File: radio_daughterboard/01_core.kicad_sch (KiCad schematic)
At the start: 11 parts, among them J1 DF40C 60-pin radio daughterbo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, U1 AP2112K-3.3 600mA daughterboa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

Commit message: Apply BOM to radio + keyboard daughterboards, add Cherry MX switch 3D models
radio_daughterboard/:
- 74 MPNs assigned (33 resistors, 41 caps) across 4 schematic sheets
- 129 BOM gaps reduced to 7 (mounting holes H1-H4, DNP connectors J44/J72/J330)

12_keyboard_daughterboard/:
- 134 MPNs assigned: 65× 1N4148W-7-F diodes, 65× Cherry MX4A-L1NA switches,
  2× caps, 2× connectors
- BOM gaps eliminated: 134 → 0

3D models:
- Added Cherry_MX_ULP_SMD.step to ducktop2.3dshapes/ (65 Cherry MX switch
  footprints on keyboard daughterboard now have 3D models)
- Created gen/add_pcb_3d_models.py script for future 3D model assignments
- 57 footprints remain without models (MountingHole, TestPoint, Tag-Connect,
  and custom ducktop2 components — need manufacturer STEP files)

gen/:
- apply_bom_radio_daughterboard.py: radio daughterboard BOM catalog
- apply_bom_keyboard_daughterboard.py: keyboard daughterboard BOM catalog
- add_pcb_3d_models.py: automated 3D model path inserter
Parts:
- C1, C4: MPN (none) -> GRM31CR71E106KA12L; Manufacturer (none) -> Murata
- C2, C3: MPN (none) -> GRM21BR71A105KA01L; Manufacturer (none) -> Murata
- C5: MPN (none) -> GRM188R71H104KA93D; Manufacturer (none) -> Murata
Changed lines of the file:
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@@
   (property "Footprint" "Capacitor_SMD:C_1206_3216Metric" (at 400.05 88.9 0) (effects (font (size 1.27 1.27)) (hide yes)))
   (property "Datasheet" "" (at 400.05 88.9 0) (effects (font (size 1.27 1.27)) (hide yes)))
+  (property "Manufacturer" "Murata" (at 400.05 88.9 0) (effects (font (size 1.27 1.27)) (hide yes)))
+  (property "MPN" "GRM31CR71E106KA12L" (at 400.05 88.9 0) (effects (font (size 1.27 1.27)) (hide yes)))
   (pin "1")
   (pin "2")
@@
   (property "Footprint" "Capacitor_SMD:C_0805_2012Metric" (at 400.05 101.6 0) (effects (font (size 1.27 1.27)) (hide yes)))
   (property "Datasheet" "" (at 400.05 101.6 0) (effects (font (size 1.27 1.27)) (hide yes)))
+  (property "Manufacturer" "Murata" (at 400.05 101.6 0) (effects (font (size 1.27 1.27)) (hide yes)))
+  (property "MPN" "GRM21BR71A105KA01L" (at 400.05 101.6 0) (effects (font (size 1.27 1.27)) (hide yes)))
   (pin "1")
   (pin "2")
@@
   (property "Footprint" "Capacitor_SMD:C_0805_2012Metric" (at 400.05 114.3 0) (effects (font (size 1.27 1.27)) (hide yes)))
   (property "Datasheet" "" (at 400.05 114.3 0) (effects (font (size 1.27 1.27)) (hide yes)))
+  (property "Manufacturer" "Murata" (at 400.05 114.3 0) (effects (font (size 1.27 1.27)) (hide yes)))
+  (property "MPN" "GRM21BR71A105KA01L" (at 400.05 114.3 0) (effects (font (size 1.27 1.27)) (hide yes)))
   (pin "1")
   (pin "2")
@@
   (property "Footprint" "Capacitor_SMD:C_1206_3216Metric" (at 400.05 127 0) (effects (font (size 1.27 1.27)) (hide yes)))
   (property "Datasheet" "" (at 400.05 127 0) (effects (font (size 1.27 1.27)) (hide yes)))
+  (property "Manufacturer" "Murata" (at 400.05 127 0) (effects (font (size 1.27 1.27)) (hide yes)))
+  (property "MPN" "GRM31CR71E106KA12L" (at 400.05 127 0) (effects (font (size 1.27 1.27)) (hide yes)))
   (pin "1")
   (pin "2")
@@
   (property "Footprint" "Capacitor_SMD:C_0603_1608Metric" (at 400.05 139.7 0) (effects (font (size 1.27 1.27)) (hide yes)))
   (property "Datasheet" "" (at 400.05 139.7 0) (effects (font (size 1.27 1.27)) (hide yes)))
+  (property "Manufacturer" "Murata" (at 400.05 139.7 0) (effects (font (size 1.27 1.27)) (hide yes)))
+  (property "MPN" "GRM188R71H104KA93D" (at 400.05 139.7 0) (effects (font (size 1.27 1.27)) (hide yes)))
   (pin "1")
   (pin "2")

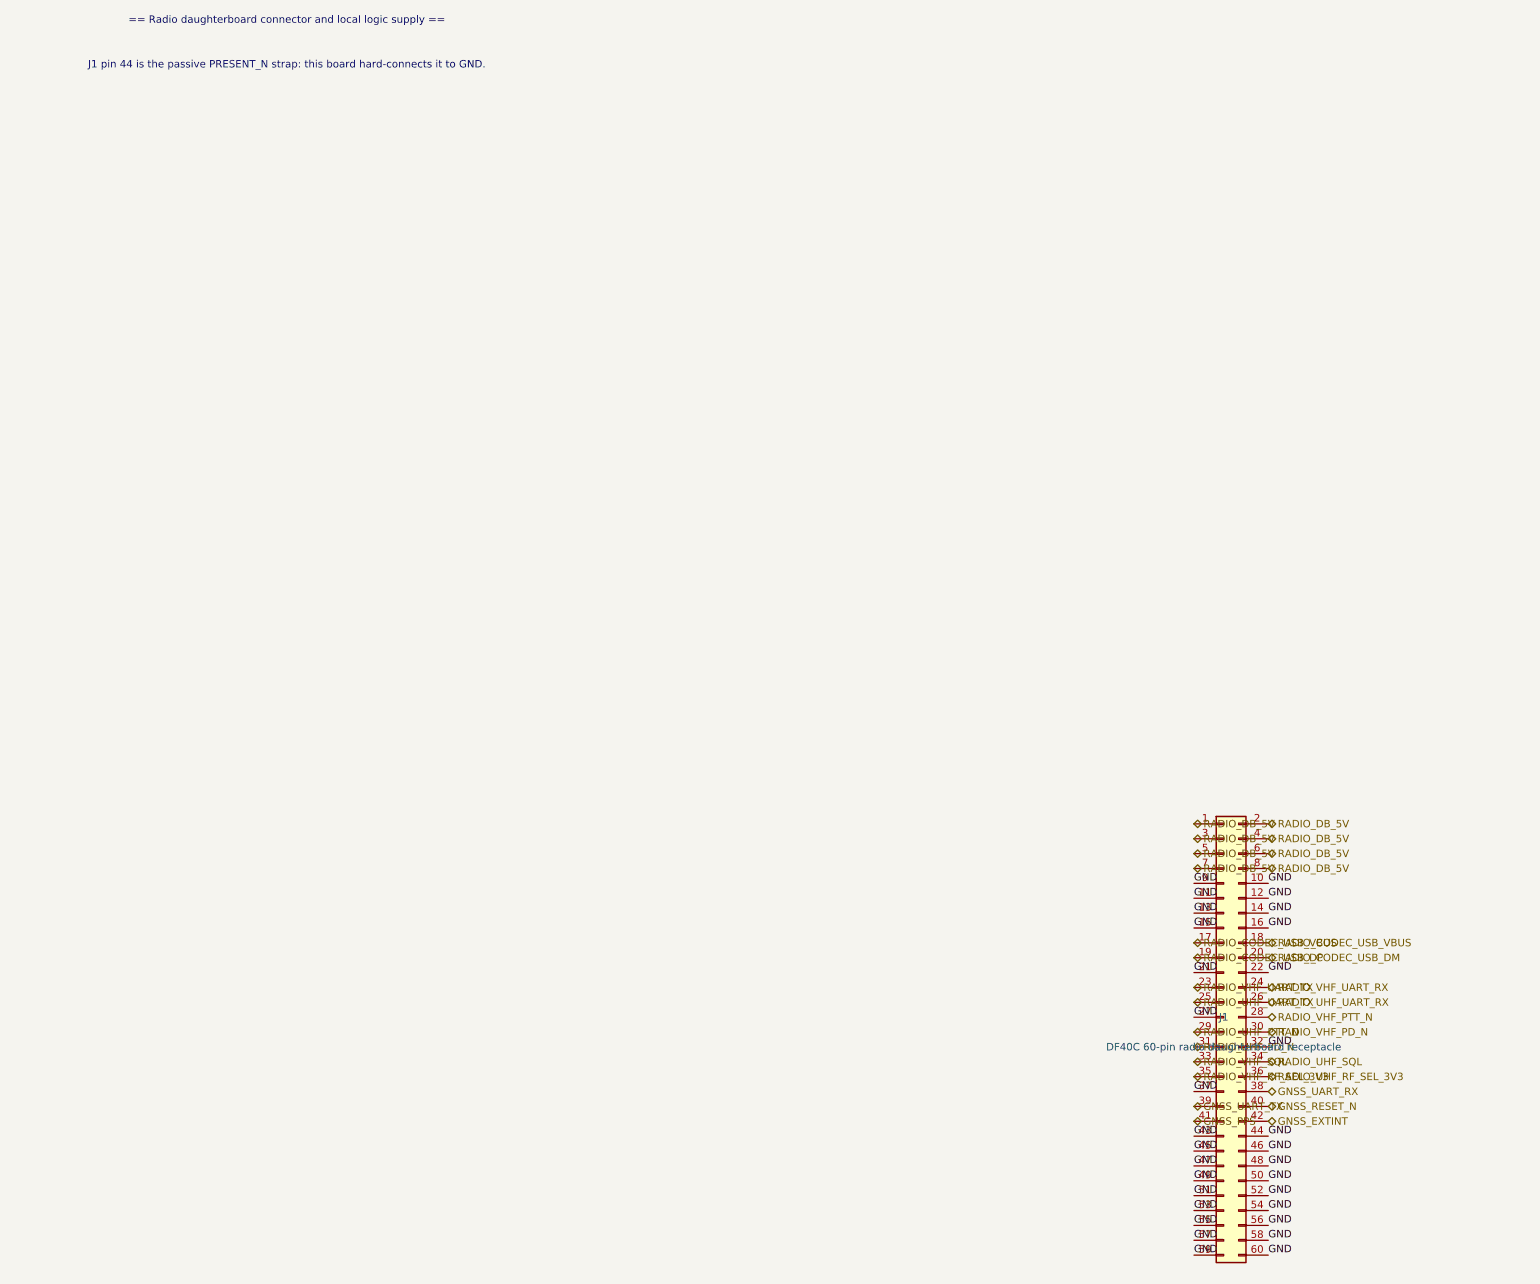
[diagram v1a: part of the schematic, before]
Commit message: Complete EC DFU port (J73) + DB power rework; verify schematic and board
- Add rear USB-C EC firmware programming port J73 (UFP/DFU) on Internal
  Services sheet: USBLC6-2P6 ESD (U63), 5.1k CC Rd resistors (R205/R211),
  22R series on D+/D- (R203/R204), mux-select hookup so BOOT0 high forces
  the USB mux to the DFU port
- Rename port ref J70->J73 after ham-radio collision; sync all net names
  (J73_CC1/J73_CC2)
- DB power rework: S5 gating + 3V3_STBY split, dual DCDC paths, GND
  returns on the standby rails; regenerate all sheets and re-verify
- sync_main_pcb_from_netlist: anchor placement for the 9 new footprints,
  scoped ECO support
- Board: rebuild main PCB with J73 footprint block (lib-sourced, net
  injection from netlist name attribute), sync pad nets for the 5 stale
  refs, remove duplicate R205/R211 copies
- Verified: check_schematic self-check OK (0 errors), radio DB contracts
  OK, ERC 0 errors, board DRC 0 electrical violations, board-vs-schematic
  net parity 0 conflicts, no duplicate refs
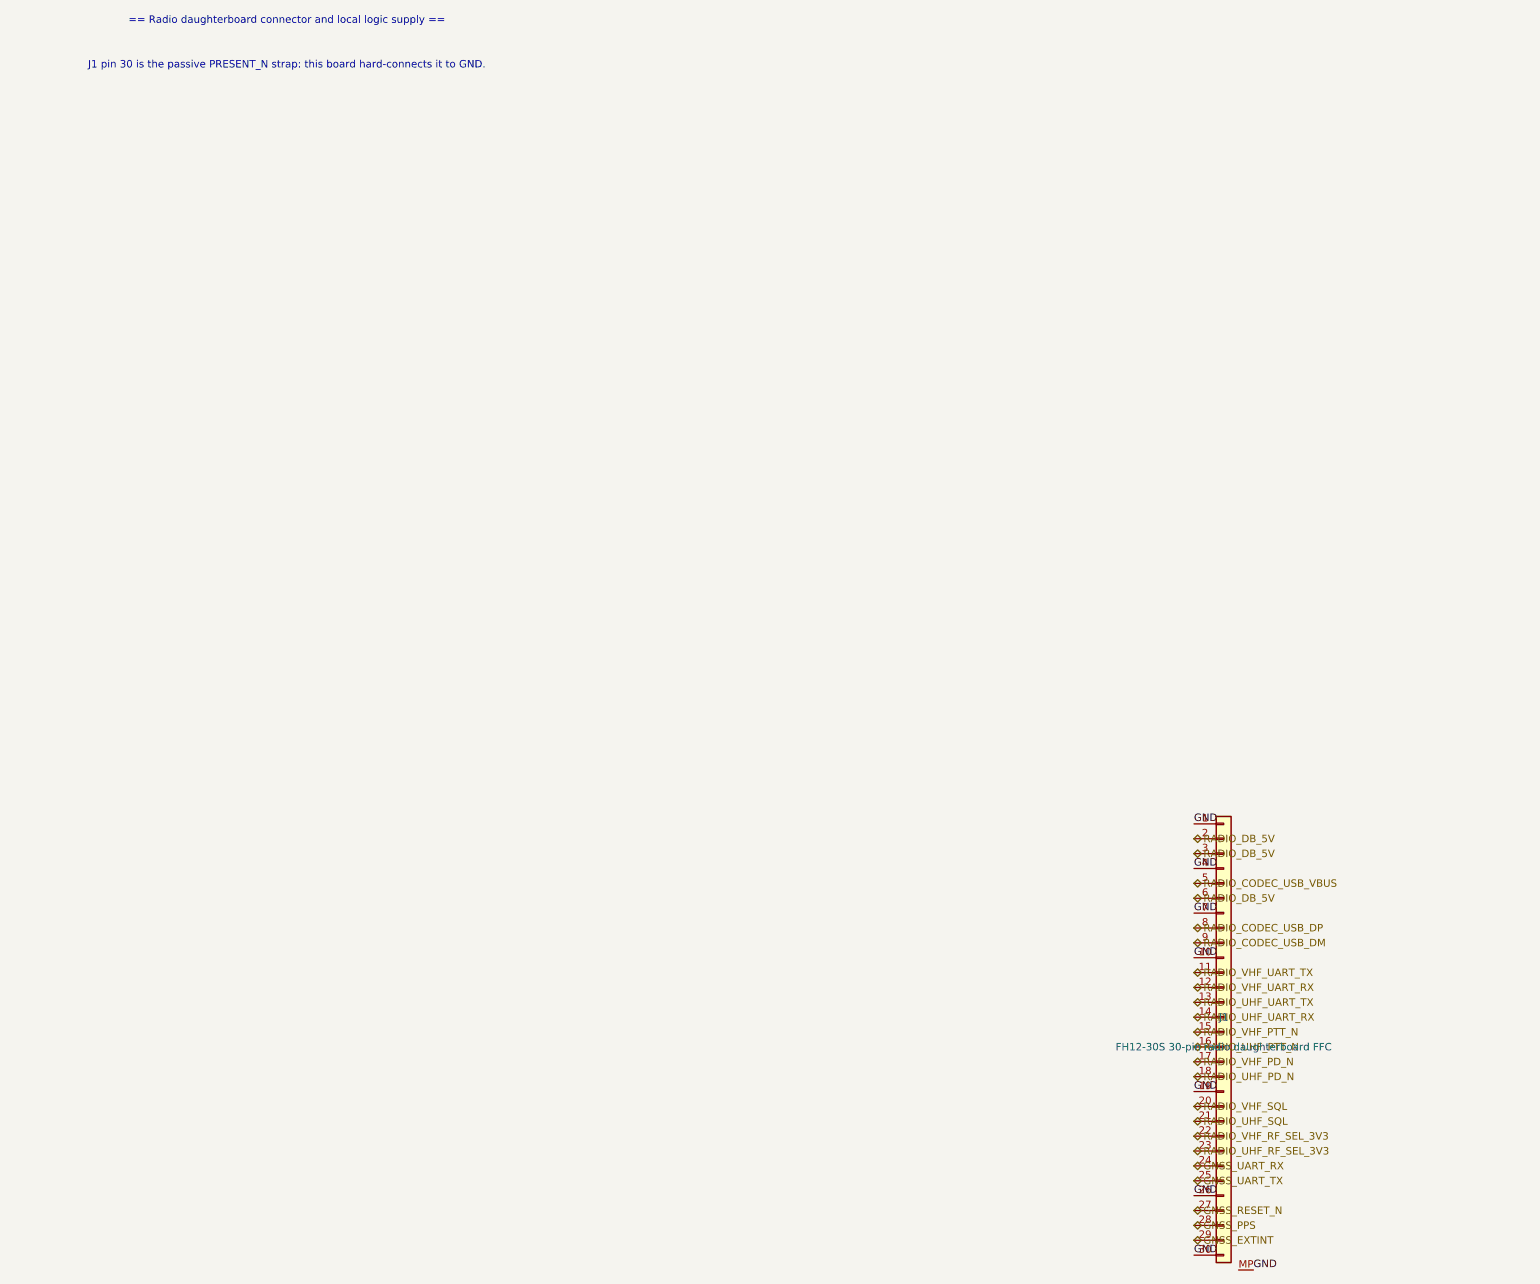
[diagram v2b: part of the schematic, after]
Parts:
- C1, C4: MPN GRM31CR71E106KA12L -> (none); Manufacturer Murata -> (none)
- C2, C3: MPN GRM21BR71A105KA01L -> (none); Manufacturer Murata -> (none)
- C5: MPN GRM188R71H104KA93D -> (none); Manufacturer Murata -> (none)
- H1, H2, H3, H4: MechanicalRole Required daughterboard support; do not rely on DF40 connect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 -> Required daughterboard support; do not rely on FFC connecto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
- J1: value DF40C 60-pin radio daughterboard receptacle -> FH12-30S 30-pin radio daughterboard FFC; footprint Connector_Hirose_DF40:Hirose_DF40C(2.0)-60DS-0.4V_2x30_P0.4mm -> Connector_FFC-FPC:Hirose_FH12-30S-0.5SH_1x30-1MP_P0.50mm_Horizontal; symbol Connector_Generic:Conn_02x30_Odd_Even -> Conn_01x30_FFC_MP:Conn_01x30_FFC_MP; MPN DF40C(2.0)-60DS-0.4V(51) -> FH12-30S-0.5SH(55); MatingConnector DF40C-60DP-0.4V(51) -> FH12 series 30-pin 0.5mm-pitch FFC cable
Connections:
- net GND: now also J1.1 (Pin_1), J1.19 (Pin_19), J1.26 (Pin_26), J1.30 (Pin_30), J1.4 (Pin_4), J1.7 (Pin_7), J1.MP; no longer J1.11 (Pin_11), J1.12 (Pin_12), J1.13 (Pin_13), J1.14 (Pin_14), J1.15 (Pin_15), J1.16 (Pin_16), J1.21 (Pin_21), J1.22 (Pin_22), J1.27 (Pin_27), J1.32 (Pin_32), J1.37 (Pin_37), J1.43 (Pin_43), J1.44 (Pin_44), J1.45 (Pin_45), J1.46 (Pin_46), J1.47 (Pin_47), J1.48 (Pin_48), J1.49 (Pin_49), J1.50 (Pin_50), J1.51 (Pin_51), J1.52 (Pin_52), J1.53 (Pin_53), J1.54 (Pin_54), J1.55 (Pin_55), J1.56 (Pin_56), J1.57 (Pin_57), J1.58 (Pin_58), J1.59 (Pin_59), J1.60 (Pin_60), J1.9 (Pin_9)
- net GNSS_EXTINT: now also J1.29 (Pin_29); no longer J1.42 (Pin_42)
- net GNSS_PPS: now also J1.28 (Pin_28); no longer J1.41 (Pin_41)
- net GNSS_RESET_N: now also J1.27 (Pin_27); no longer J1.40 (Pin_40)
- net GNSS_UART_RX: now also J1.24 (Pin_24); no longer J1.38 (Pin_38)
- net GNSS_UART_TX: now also J1.25 (Pin_25); no longer J1.39 (Pin_39)
- net RADIO_CODEC_USB_DM: now also J1.9 (Pin_9); no longer J1.20 (Pin_20)
- net RADIO_CODEC_USB_DP: now also J1.8 (Pin_8); no longer J1.19 (Pin_19)
- net RADIO_CODEC_USB_VBUS: now also J1.5 (Pin_5); no longer J1.17 (Pin_17), J1.18 (Pin_18)
- net RADIO_DB_5V: no longer J1.1 (Pin_1), J1.4 (Pin_4), J1.5 (Pin_5), J1.7 (Pin_7), J1.8 (Pin_8)
- net RADIO_UHF_PD_N: now also J1.18 (Pin_18); no longer J1.31 (Pin_31)
- net RADIO_UHF_PTT_N: now also J1.16 (Pin_16); no longer J1.29 (Pin_29)
- net RADIO_UHF_RF_SEL_3V3: now also J1.23 (Pin_23); no longer J1.36 (Pin_36)
- net RADIO_UHF_SQL: now also J1.21 (Pin_21); no longer J1.34 (Pin_34)
- net RADIO_UHF_UART_RX: now also J1.14 (Pin_14); no longer J1.26 (Pin_26)
- net RADIO_UHF_UART_TX: now also J1.13 (Pin_13); no longer J1.25 (Pin_25)
- net RADIO_VHF_PD_N: now also J1.17 (Pin_17); no longer J1.30 (Pin_30)
- net RADIO_VHF_PTT_N: now also J1.15 (Pin_15); no longer J1.28 (Pin_28)
- net RADIO_VHF_RF_SEL_3V3: now also J1.22 (Pin_22); no longer J1.35 (Pin_35)
- net RADIO_VHF_SQL: now also J1.20 (Pin_20); no longer J1.33 (Pin_33)
- net RADIO_VHF_UART_RX: now also J1.12 (Pin_12); no longer J1.24 (Pin_24)
- net RADIO_VHF_UART_TX: now also J1.11 (Pin_11); no longer J1.23 (Pin_23)
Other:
- note added: "J1 pin 30 is the passive PRESENT_N strap: this board hard-connects it to GND."
- note removed: "J1 pin 44 is the passive PRESENT_N strap: this board hard-connects it to GND."

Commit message: get the main boards ready for routing
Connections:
- net RADIO_CODEC_USB_DM renamed RADIO_CODEC_USB_DN
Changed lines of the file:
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@@
   (effects (font (size 1.27 1.27)) (justify left bottom))
 )
-(hierarchical_label "RADIO_CODEC_USB_DM"
+(hierarchical_label "RADIO_CODEC_USB_DN"
   (shape bidirectional)
   (at 175.26 170.18 0)

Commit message: fix audit issues and move some connectors
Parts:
- C1, C4: MPN (none) -> GRM31CR71E106KA12L; Manufacturer (none) -> Murata
- C2, C3: MPN (none) -> GRM21BR71A105KA01L; Manufacturer (none) -> Murata
- C5: MPN (none) -> GRM188R71H104KA93D; Manufacturer (none) -> Murata
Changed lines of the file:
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@@
   (property "Footprint" "Capacitor_SMD:C_1206_3216Metric" (at 400.05 88.9 0) (effects (font (size 1.27 1.27)) (hide yes)))
   (property "Datasheet" "" (at 400.05 88.9 0) (effects (font (size 1.27 1.27)) (hide yes)))
+  (property "Manufacturer" "Murata" (at 400.05 88.9 0) (effects (font (size 1.27 1.27)) (hide yes)))
+  (property "MPN" "GRM31CR71E106KA12L" (at 400.05 88.9 0) (effects (font (size 1.27 1.27)) (hide yes)))
   (pin "1")
   (pin "2")
@@
   (property "Footprint" "Capacitor_SMD:C_0805_2012Metric" (at 400.05 101.6 0) (effects (font (size 1.27 1.27)) (hide yes)))
   (property "Datasheet" "" (at 400.05 101.6 0) (effects (font (size 1.27 1.27)) (hide yes)))
+  (property "Manufacturer" "Murata" (at 400.05 101.6 0) (effects (font (size 1.27 1.27)) (hide yes)))
+  (property "MPN" "GRM21BR71A105KA01L" (at 400.05 101.6 0) (effects (font (size 1.27 1.27)) (hide yes)))
   (pin "1")
   (pin "2")
@@
   (property "Footprint" "Capacitor_SMD:C_0805_2012Metric" (at 400.05 114.3 0) (effects (font (size 1.27 1.27)) (hide yes)))
   (property "Datasheet" "" (at 400.05 114.3 0) (effects (font (size 1.27 1.27)) (hide yes)))
+  (property "Manufacturer" "Murata" (at 400.05 114.3 0) (effects (font (size 1.27 1.27)) (hide yes)))
+  (property "MPN" "GRM21BR71A105KA01L" (at 400.05 114.3 0) (effects (font (size 1.27 1.27)) (hide yes)))
   (pin "1")
   (pin "2")
@@
   (property "Footprint" "Capacitor_SMD:C_1206_3216Metric" (at 400.05 127 0) (effects (font (size 1.27 1.27)) (hide yes)))
   (property "Datasheet" "" (at 400.05 127 0) (effects (font (size 1.27 1.27)) (hide yes)))
+  (property "Manufacturer" "Murata" (at 400.05 127 0) (effects (font (size 1.27 1.27)) (hide yes)))
+  (property "MPN" "GRM31CR71E106KA12L" (at 400.05 127 0) (effects (font (size 1.27 1.27)) (hide yes)))
   (pin "1")
   (pin "2")
@@
   (property "Footprint" "Capacitor_SMD:C_0603_1608Metric" (at 400.05 139.7 0) (effects (font (size 1.27 1.27)) (hide yes)))
   (property "Datasheet" "" (at 400.05 139.7 0) (effects (font (size 1.27 1.27)) (hide yes)))
+  (property "Manufacturer" "Murata" (at 400.05 139.7 0) (effects (font (size 1.27 1.27)) (hide yes)))
+  (property "MPN" "GRM188R71H104KA93D" (at 400.05 139.7 0) (effects (font (size 1.27 1.27)) (hide yes)))
   (pin "1")
   (pin "2")
